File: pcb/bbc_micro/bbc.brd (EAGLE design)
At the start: 43 x 30 mm, 24 parts, among them U2 LM2776

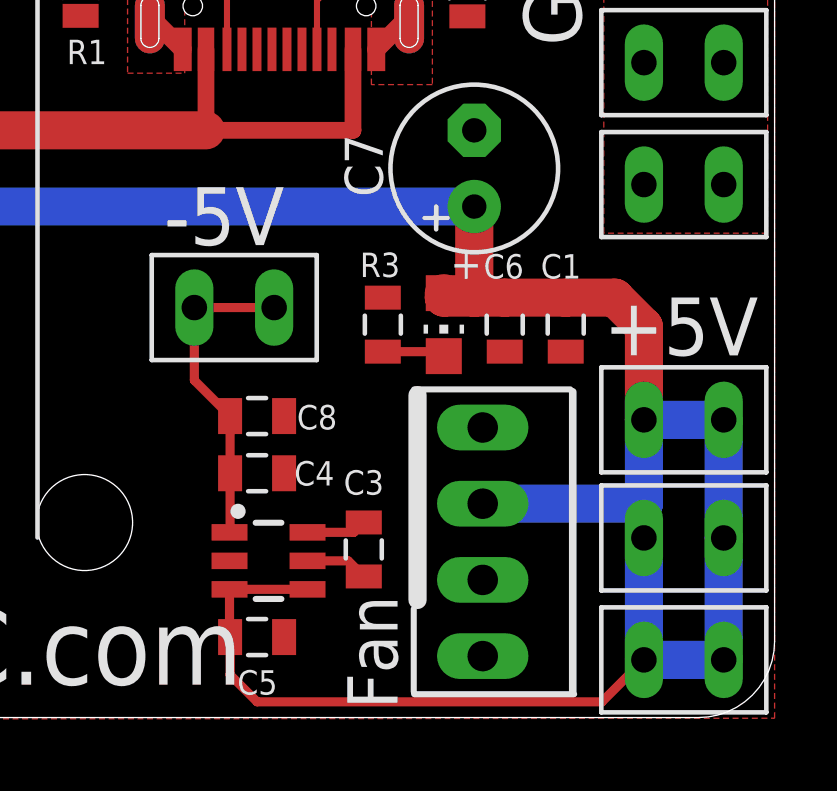
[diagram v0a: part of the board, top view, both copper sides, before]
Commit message: adjusted lm2776 footprint
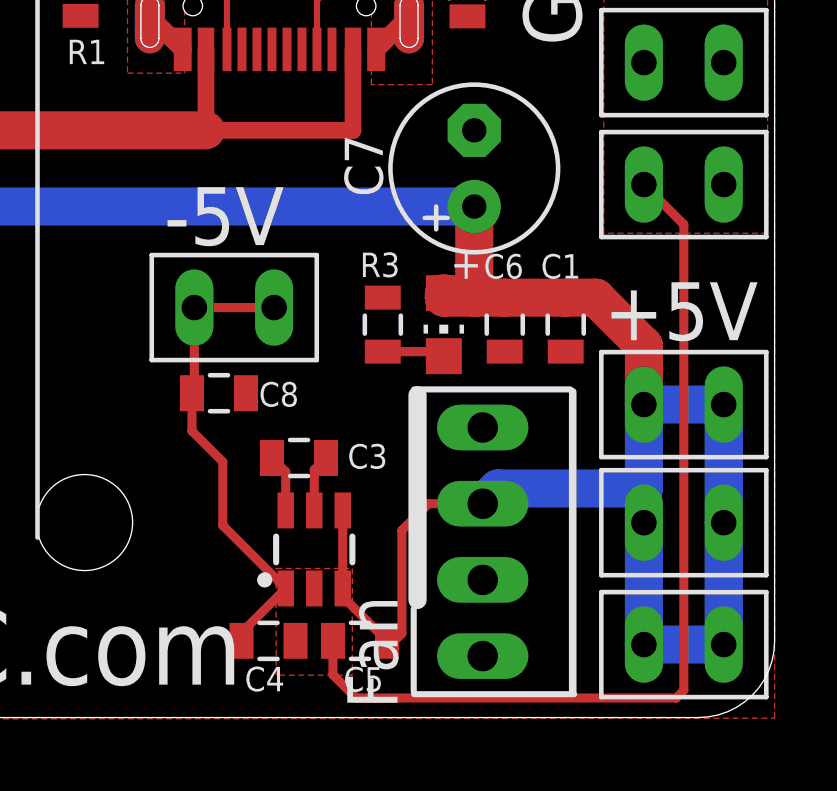
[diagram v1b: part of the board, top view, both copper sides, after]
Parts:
- moved C4 5.60 mm to (32.1, 3.56)
- moved C3 3.74 mm to (33.1, 9.65), turned to 0 degrees
- moved C5 3.43 mm to (35.2, 3.56), turned to 180 degrees
- moved U2 1.57 mm to (33.7, 6.60), turned to 0 degrees
- moved C8 1.48 mm to (30.5, 11.8)
- moved U$6 0.51 mm to (46.0, 11.4)
- moved U$7 0.51 mm to (46.0, 7.50)
- moved U$8 0.51 mm to (46.0, 3.43)
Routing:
- net GND: track 2.95 -> 33.6 mm
- net +5V: track 99.8 -> 91.0 mm
- net N$4: track 10.7 -> 15.7 mm

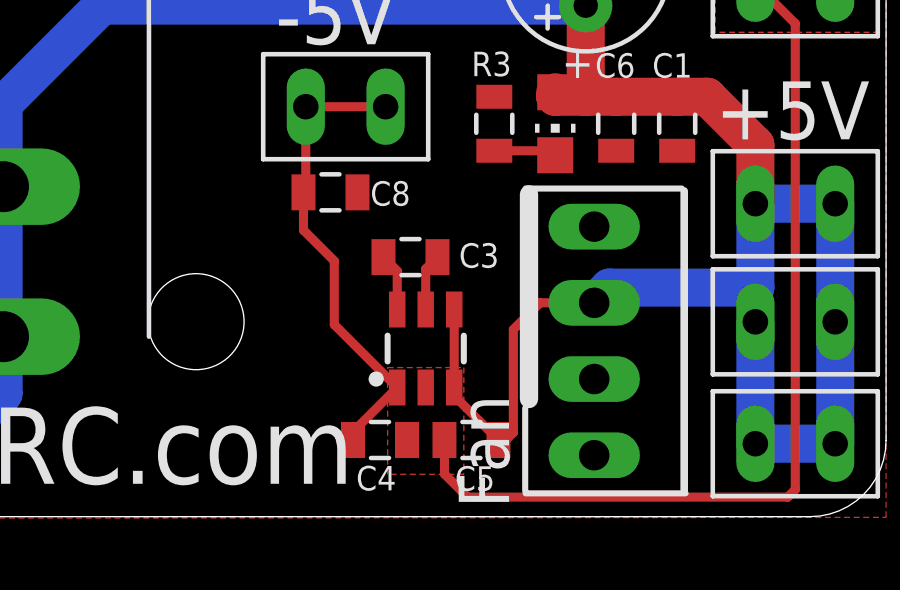
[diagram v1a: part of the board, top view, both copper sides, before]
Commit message: adjusted lm2776 footprint
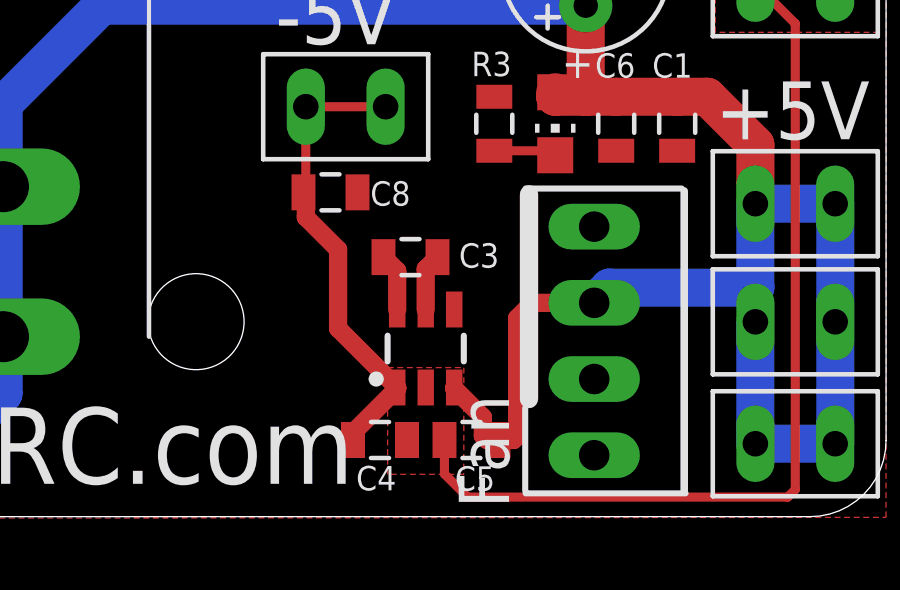
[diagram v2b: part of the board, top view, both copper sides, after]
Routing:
- net +5V: track 91.0 -> 88.9 mm
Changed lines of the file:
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@@
 <vertex x="27.305" y="27.305"/>
 </polygon>
-<polygon width="0.1524" layer="1" thermals="no">
+<polygon width="0.1524" layer="1" isolate="0.3048" thermals="no">
 <vertex x="34.925" y="5.969"/>
 <vertex x="34.925" y="2.413"/>
@@
 <wire x1="44.644" y1="8.636" x2="39.779" y2="8.636" width="1.27" layer="16"/>
 <wire x1="39.271" y1="8.128" x2="39.779" y2="8.636" width="1.27" layer="16"/>
-<wire x1="36.079" y1="3.556" x2="34.605" y2="5.03" width="0.3048" layer="1"/>
-<wire x1="34.605" y1="5.03" x2="34.605" y2="5.3039" width="0.3048" layer="1"/>
-<wire x1="34.605" y1="5.3039" x2="34.605" y2="7.9041" width="0.3048" layer="1"/>
-<wire x1="36.079" y1="3.567" x2="36.079" y2="3.556" width="0.3048" layer="1"/>
 <wire x1="42.037" y1="14.997" x2="43.042" y2="14.997" width="1.27" layer="1"/>
 <wire x1="43.042" y1="14.997" x2="44.644" y2="13.395" width="1.27" layer="1"/>
-<wire x1="39.271" y1="8.128" x2="37.465" y2="8.128" width="0.3048" layer="1"/>
-<wire x1="37.465" y1="8.128" x2="36.576" y2="7.239" width="0.3048" layer="1"/>
-<wire x1="36.576" y1="7.239" x2="36.576" y2="3.799" width="0.3048" layer="1"/>
-<wire x1="36.576" y1="3.799" x2="36.333" y2="3.556" width="0.3048" layer="1"/>
-<wire x1="36.333" y1="3.556" x2="36.079" y2="3.556" width="0.3048" layer="1"/>
+<wire x1="39.271" y1="8.128" x2="37.211" y2="8.128" width="0.6096" layer="1"/>
+<wire x1="37.211" y1="8.128" x2="36.703" y2="7.62" width="0.6096" layer="1"/>
+<wire x1="36.703" y1="3.672" x2="36.587" y2="3.556" width="0.6096" layer="1"/>
+<wire x1="36.079" y1="3.556" x2="36.587" y2="3.556" width="0.6096" layer="1"/>
+<wire x1="36.703" y1="7.62" x2="36.703" y2="3.672" width="0.6096" layer="1"/>
+<wire x1="34.605" y1="5.3039" x2="34.605" y2="5.273" width="0.6096" layer="1"/>
+<wire x1="35.56" y1="4.318" x2="34.605" y2="5.273" width="0.6096" layer="1"/>
+<wire x1="35.56" y1="4.318" x2="35.56" y2="3.694" width="0.6096" layer="1"/>
+<wire x1="35.698" y1="3.556" x2="35.56" y2="3.694" width="0.6096" layer="1"/>
+<wire x1="35.698" y1="3.556" x2="36.079" y2="3.556" width="0.6096" layer="1"/>
+<wire x1="34.605" y1="5.3039" x2="34.605" y2="7.9041" width="0" layer="19" extent="1-1"/>
 </signal>
 <signal name="N$31">
@@
 <contactref element="U2" pad="5"/>
 <contactref element="C3" pad="2"/>
-<wire x1="33.655" y1="7.9041" x2="33.655" y2="9.26" width="0.3048" layer="1"/>
-<wire x1="33.655" y1="9.26" x2="34.047" y2="9.652" width="0.3048" layer="1"/>
+<wire x1="33.655" y1="7.9041" x2="33.655" y2="9.26" width="0.6096" layer="1"/>
+<wire x1="33.655" y1="9.26" x2="34.047" y2="9.652" width="0.6096" layer="1"/>
 </signal>
 <signal name="N$3">
 <contactref element="C3" pad="1"/>
 <contactref element="U2" pad="6"/>
-<wire x1="32.705" y1="7.9041" x2="32.705" y2="9.194" width="0.3048" layer="1"/>
-<wire x1="32.705" y1="9.194" x2="32.247" y2="9.652" width="0.3048" layer="1"/>
+<wire x1="32.705" y1="7.9041" x2="32.705" y2="9.194" width="0.6096" layer="1"/>
+<wire x1="32.705" y1="9.194" x2="32.247" y2="9.652" width="0.6096" layer="1"/>
 </signal>
 <signal name="N$4">
@@
 <contactref element="U$5" pad="P$2"/>
 <wire x1="29.658" y1="14.666" x2="32.318" y2="14.666" width="0.3048" layer="1"/>
-<wire x1="32.705" y1="5.3039" x2="31.231" y2="3.8299" width="0.3048" layer="1"/>
-<wire x1="31.231" y1="3.8299" x2="31.231" y2="3.556" width="0.3048" layer="1"/>
-<wire x1="32.705" y1="5.3039" x2="30.607" y2="7.4019" width="0.3048" layer="1"/>
-<wire x1="30.607" y1="7.4019" x2="30.607" y2="9.525" width="0.3048" layer="1"/>
-<wire x1="30.607" y1="9.525" x2="29.58" y2="10.552" width="0.3048" layer="1"/>
-<wire x1="29.58" y1="10.552" x2="29.58" y2="11.811" width="0.3048" layer="1"/>
 <wire x1="29.658" y1="14.666" x2="29.658" y2="11.889" width="0.3048" layer="1"/>
 <wire x1="29.658" y1="11.889" x2="29.58" y2="11.811" width="0.3048" layer="1"/>
+<wire x1="31.231" y1="3.556" x2="31.231" y2="3.799" width="0.6096" layer="1"/>
+<wire x1="32.705" y1="5.273" x2="32.705" y2="5.3039" width="0.6096" layer="1"/>
+<wire x1="31.231" y1="3.799" x2="32.705" y2="5.273" width="0.6096" layer="1"/>
+<wire x1="32.705" y1="5.3039" x2="30.734" y2="7.2749" width="0.6096" layer="1"/>
+<wire x1="30.734" y1="7.2749" x2="30.734" y2="9.906" width="0.6096" layer="1"/>
+<wire x1="30.734" y1="9.906" x2="29.658" y2="10.982" width="0.6096" layer="1"/>
+<wire x1="29.658" y1="10.982" x2="29.658" y2="11.889" width="0.6096" layer="1"/>
 </signal>
 </signals>

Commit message: updated PCB
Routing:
- net +5V: track 88.9 -> 90.7 mm
- net N$4: track 15.8 -> 17.3 mm
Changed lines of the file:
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@@
 <wire x1="42.037" y1="14.997" x2="43.042" y2="14.997" width="1.27" layer="1"/>
 <wire x1="43.042" y1="14.997" x2="44.644" y2="13.395" width="1.27" layer="1"/>
-<wire x1="39.271" y1="8.128" x2="37.211" y2="8.128" width="0.6096" layer="1"/>
-<wire x1="37.211" y1="8.128" x2="36.703" y2="7.62" width="0.6096" layer="1"/>
-<wire x1="36.703" y1="3.672" x2="36.587" y2="3.556" width="0.6096" layer="1"/>
-<wire x1="36.079" y1="3.556" x2="36.587" y2="3.556" width="0.6096" layer="1"/>
-<wire x1="36.703" y1="7.62" x2="36.703" y2="3.672" width="0.6096" layer="1"/>
-<wire x1="34.605" y1="5.3039" x2="34.605" y2="5.273" width="0.6096" layer="1"/>
-<wire x1="35.56" y1="4.318" x2="34.605" y2="5.273" width="0.6096" layer="1"/>
-<wire x1="35.56" y1="4.318" x2="35.56" y2="3.694" width="0.6096" layer="1"/>
-<wire x1="35.698" y1="3.556" x2="35.56" y2="3.694" width="0.6096" layer="1"/>
-<wire x1="35.698" y1="3.556" x2="36.079" y2="3.556" width="0.6096" layer="1"/>
-<wire x1="34.605" y1="5.3039" x2="34.605" y2="7.9041" width="0" layer="19" extent="1-1"/>
+<wire x1="39.271" y1="8.128" x2="38.1" y2="8.128" width="0.4064" layer="1"/>
+<wire x1="36.83" y1="6.858" x2="38.1" y2="8.128" width="0.4064" layer="1"/>
+<wire x1="34.605" y1="5.3039" x2="34.605" y2="5.03" width="0.4064" layer="1"/>
+<wire x1="34.605" y1="5.03" x2="36.079" y2="3.556" width="0.4064" layer="1"/>
+<wire x1="36.079" y1="3.556" x2="36.206" y2="3.683" width="0.4064" layer="1"/>
+<wire x1="36.206" y1="3.683" x2="36.576" y2="3.683" width="0.4064" layer="1"/>
+<wire x1="36.576" y1="3.683" x2="36.83" y2="3.937" width="0.4064" layer="1"/>
+<wire x1="36.83" y1="3.937" x2="36.83" y2="6.858" width="0.4064" layer="1"/>
+<wire x1="34.605" y1="5.3039" x2="34.605" y2="7.9041" width="0.4064" layer="1"/>
 </signal>
 <signal name="N$31">
@@
 <contactref element="U2" pad="5"/>
 <contactref element="C3" pad="2"/>
-<wire x1="33.655" y1="7.9041" x2="33.655" y2="9.26" width="0.6096" layer="1"/>
+<wire x1="33.655" y1="7.9041" x2="33.655" y2="9.26" width="0.508" layer="1"/>
 <wire x1="33.655" y1="9.26" x2="34.047" y2="9.652" width="0.6096" layer="1"/>
 </signal>
@@
 <contactref element="C3" pad="1"/>
 <contactref element="U2" pad="6"/>
-<wire x1="32.705" y1="7.9041" x2="32.705" y2="9.194" width="0.6096" layer="1"/>
+<wire x1="32.705" y1="7.9041" x2="32.705" y2="9.194" width="0.508" layer="1"/>
 <wire x1="32.705" y1="9.194" x2="32.247" y2="9.652" width="0.6096" layer="1"/>
 </signal>
@@
 <wire x1="29.658" y1="14.666" x2="29.658" y2="11.889" width="0.3048" layer="1"/>
 <wire x1="29.658" y1="11.889" x2="29.58" y2="11.811" width="0.3048" layer="1"/>
-<wire x1="31.231" y1="3.556" x2="31.231" y2="3.799" width="0.6096" layer="1"/>
-<wire x1="32.705" y1="5.273" x2="32.705" y2="5.3039" width="0.6096" layer="1"/>
-<wire x1="31.231" y1="3.799" x2="32.705" y2="5.273" width="0.6096" layer="1"/>
-<wire x1="32.705" y1="5.3039" x2="30.734" y2="7.2749" width="0.6096" layer="1"/>
-<wire x1="30.734" y1="7.2749" x2="30.734" y2="9.906" width="0.6096" layer="1"/>
-<wire x1="30.734" y1="9.906" x2="29.658" y2="10.982" width="0.6096" layer="1"/>
-<wire x1="29.658" y1="10.982" x2="29.658" y2="11.889" width="0.6096" layer="1"/>
+<wire x1="32.705" y1="5.3039" x2="32.004" y2="4.6029" width="0.4064" layer="1"/>
+<wire x1="32.004" y1="4.6029" x2="32.004" y2="3.937" width="0.4064" layer="1"/>
+<wire x1="32.004" y1="3.937" x2="31.623" y2="3.556" width="0.4064" layer="1"/>
+<wire x1="31.623" y1="3.556" x2="31.231" y2="3.556" width="0.4064" layer="1"/>
+<wire x1="31.231" y1="3.556" x2="30.861" y2="3.556" width="0.4064" layer="1"/>
+<wire x1="30.48" y1="10.403" x2="29.58" y2="11.303" width="0.4064" layer="1"/>
+<wire x1="29.58" y1="11.303" x2="29.58" y2="11.811" width="0.4064" layer="1"/>
+<wire x1="30.861" y1="3.556" x2="30.48" y2="3.937" width="0.4064" layer="1"/>
+<wire x1="30.48" y1="3.937" x2="30.48" y2="10.403" width="0.4064" layer="1"/>
 </signal>
 </signals>

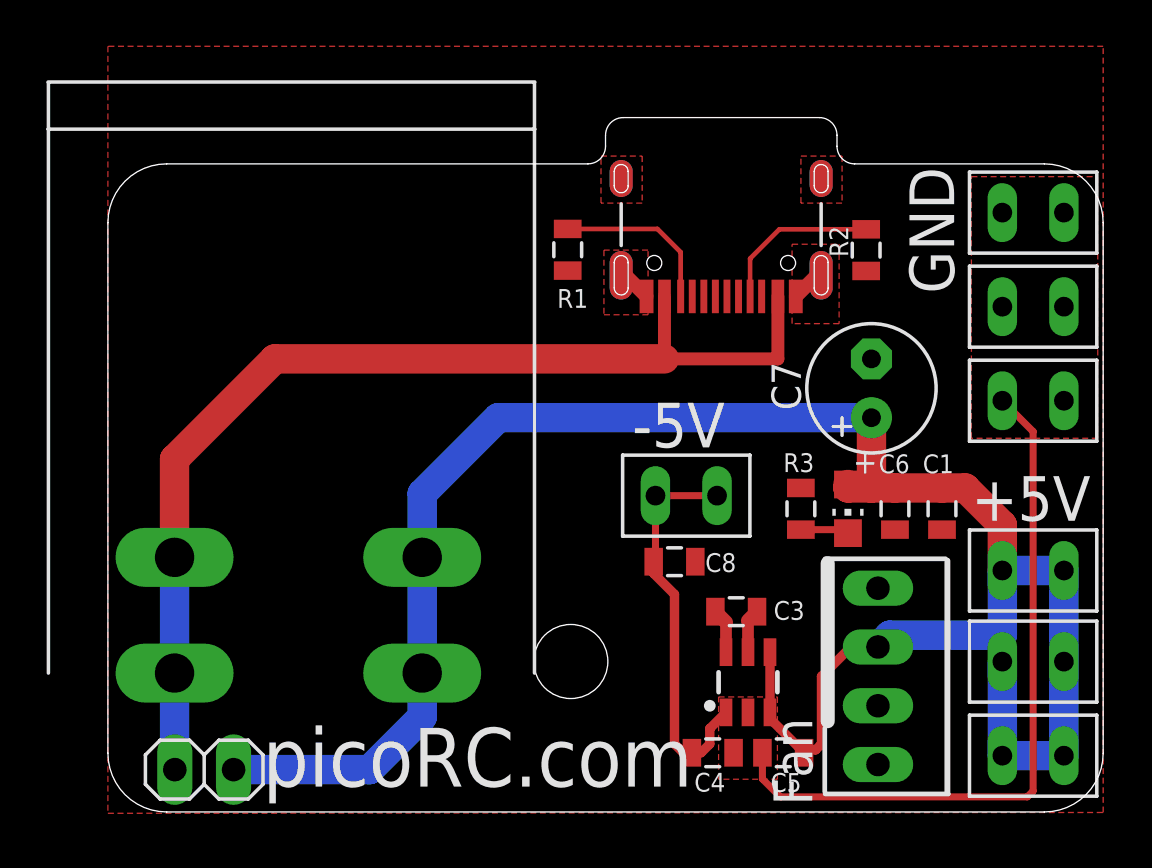
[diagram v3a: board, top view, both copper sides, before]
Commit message: updated BBC micro PCB
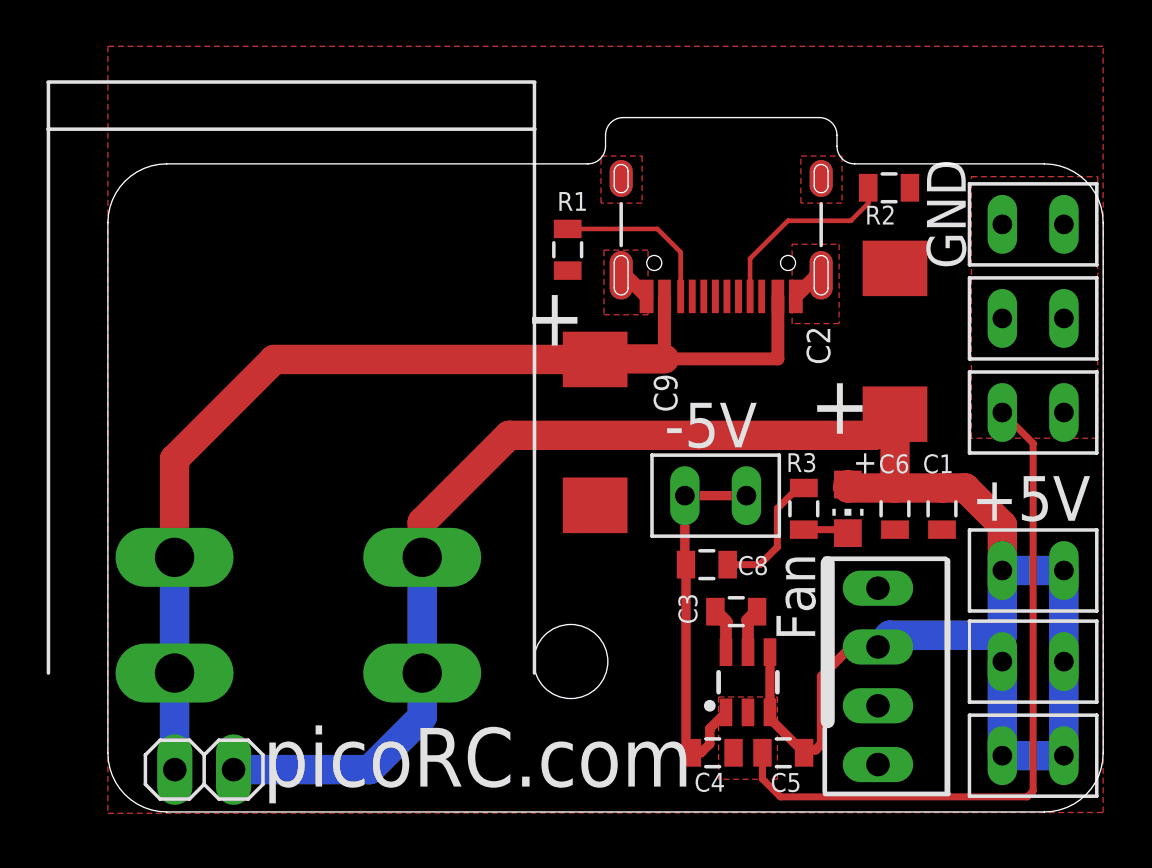
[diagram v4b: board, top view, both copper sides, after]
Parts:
- removed C7: (no value), adafruit:E2,5-6
- added C2, C9: 470uF, rcl:SMC_D
- moved R2 2.87 mm to (39.8, 28.0), turned to 0 degrees
- moved C8 1.40 mm to (31.9, 11.7)
- moved U$5 1.27 mm to (32.3, 14.7)
- moved U$10 0.51 mm to (46.0, 22.3)
- moved U$11 0.51 mm to (46.0, 18.3)
- moved U$9 0.51 mm to (46.0, 26.4)
- moved R3 0.13 mm to (36.1, 14.1)
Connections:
- net +5V: now also C2.+; no longer C7.+
- net GND: now also C2.-, C9.-; no longer C7.-
- net N$1: now also C9.+
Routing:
- net GND: track 33.6 -> 38.7 mm
- net N$6: track 7.17 -> 8.40 mm
- net N$4: track 17.3 -> 16.5 mm
- net +5V: track 90.7 -> 91.2 mm
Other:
- board text added: "+"
- board text added: "PT4 dekuNukem MAY 2023"
- board text removed: "PD1 dekuNukem APR 2023"
